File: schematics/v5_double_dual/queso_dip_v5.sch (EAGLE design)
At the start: 41 parts, among them K1 61400826021, K2 61400826021, Q1 FOXSDLF/120-20, U1 PRTR5V0U2X,215, U2 PRTR5V0U2X,215, U3 PRTR5V0U2X,215, U4 PRTR5V0U2X,215, U5 PRTR5V0U2X,215

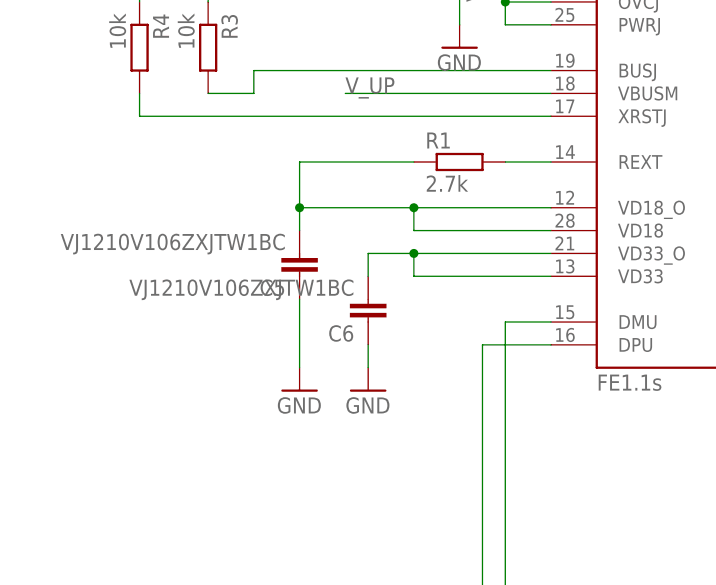
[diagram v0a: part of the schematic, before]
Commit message: ordered v4 with correct vss
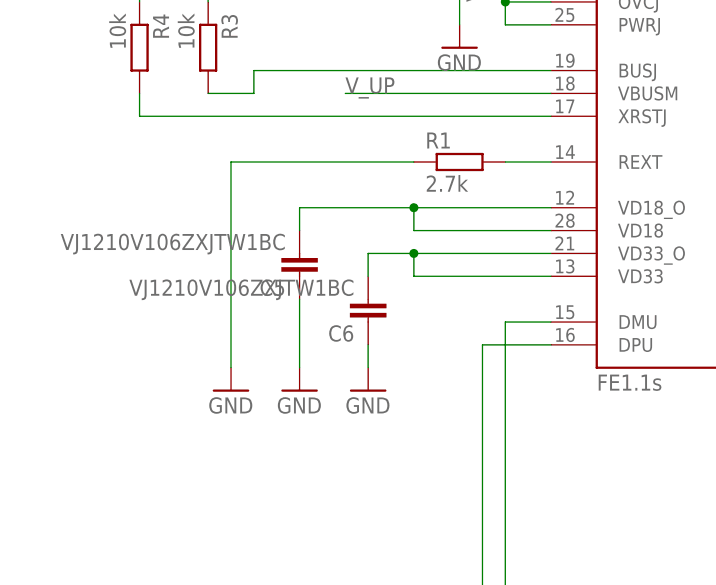
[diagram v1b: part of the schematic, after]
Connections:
- net GND: now also R1.1
- net N$18: no longer R1.1
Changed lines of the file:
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@@
 <part name="K1" library="Wuerth_Elektronik_eiCan_Communication_Connectors_STENCIL" deviceset="61400826021" device=""/>
 <part name="K2" library="Wuerth_Elektronik_eiCan_Communication_Connectors_STENCIL" deviceset="61400826021" device=""/>
+<part name="GND14" library="supply1" deviceset="GND" device=""/>
 </parts>
 <sheets>
@@
 <instance part="K1" gate="G$1" x="256.54" y="157.48"/>
 <instance part="K2" gate="G$1" x="256.54" y="121.92"/>
+<instance part="GND14" gate="1" x="45.72" y="149.86"/>
 </instances>
 <busses>
@@
 <pinref part="C7" gate="G$1" pin="1"/>
 <pinref part="GND21" gate="1" pin="GND"/>
+</segment>
+<segment>
+<pinref part="R1" gate="G$1" pin="1"/>
+<wire x1="66.04" y1="175.26" x2="45.72" y2="175.26" width="0.1524" layer="91"/>
+<pinref part="GND14" gate="1" pin="GND"/>
+<wire x1="45.72" y1="175.26" x2="45.72" y2="152.4" width="0.1524" layer="91"/>
 </segment>
 </net>
@@
 <wire x1="66.04" y1="167.64" x2="66.04" y2="170.18" width="0.1524" layer="91"/>
 <junction x="66.04" y="170.18"/>
-<pinref part="R1" gate="G$1" pin="1"/>
-<wire x1="66.04" y1="175.26" x2="53.34" y2="175.26" width="0.1524" layer="91"/>
-<wire x1="53.34" y1="175.26" x2="53.34" y2="170.18" width="0.1524" layer="91"/>
-<junction x="53.34" y="170.18"/>
-</segment>
-</net>
+</segment>
+</net>
